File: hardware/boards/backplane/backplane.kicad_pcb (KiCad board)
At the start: 4 copper layers, 151.8 x 30.8 mm, 89 parts, among them J1 XT30U_2+2, J10 SWD, J11 12V 3-WIRE FAN, J12 DS18B20 EXT SUPPLY, J2 XT30U_2+2, J3 XT30U_2+2, J4 XT30U_2+2, J5 XT30U_2+2, J6 XT30U_2+2, J7 XY308-2.54-3P / EXTERNAL CAN, J8 DC IN, J9 12V 3-WIRE FAN, Q1 AO3407A, Q2 2N7002, Q3 AO3407A, Q4 2N7002, U1 STM32C092GCU6, U2 LM5164DDAR, U3 LM5164DDAR, U4 INA237AIDGSR, U5 TCAN3413DR

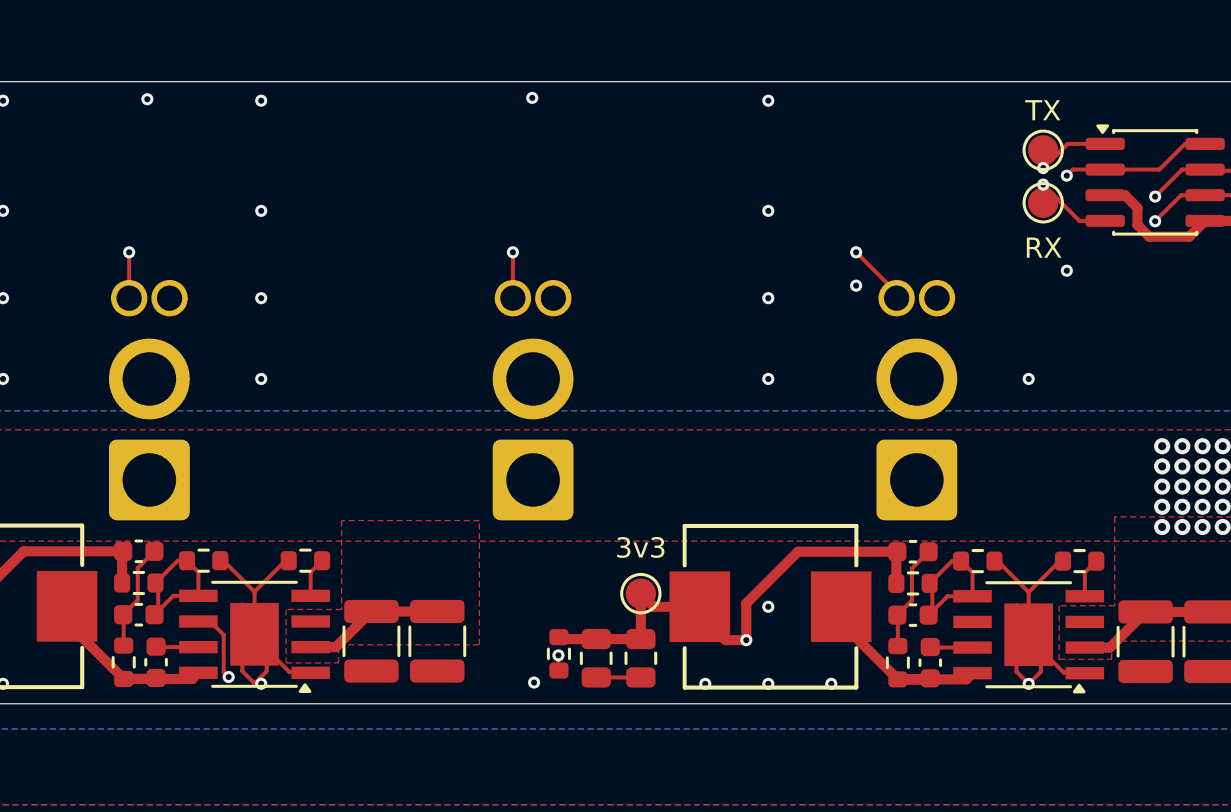
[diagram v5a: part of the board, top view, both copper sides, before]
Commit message: Checkpoint backplane before CAN test point routing adjustments
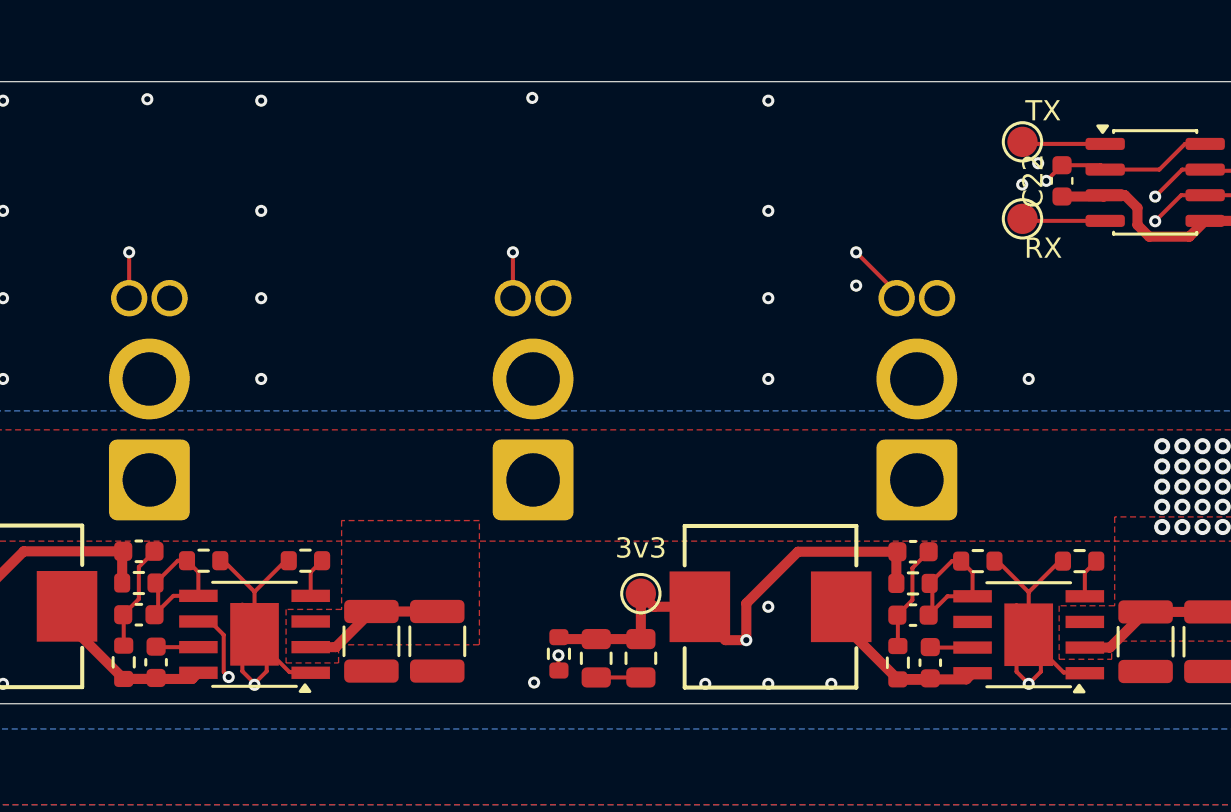
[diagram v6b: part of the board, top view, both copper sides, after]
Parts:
- added C22: 100nF, Capacitor_SMD:C_0603_1608Metric, F.Cu at (149.2, 51.6)
- moved TP7 1.30 mm to (147.2, 53.5)
- moved TP6 1.11 mm to (147.2, 49.7)
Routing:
- net +3V3: track 291.9 -> 294.0 mm
- net GND: track 56.7 -> 57.7 mm, vias 67 -> 66
- net CAN_RX: track 94.3 -> 93.5 mm

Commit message: Align CAN test points and clean up U5 routing and silkscreen
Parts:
- moved TP6 2.04 mm to (145.2, 49.8)
- moved TP7 2.04 mm to (145.2, 53.6)
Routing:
- net CAN_RX: track 93.5 -> 94.3 mm
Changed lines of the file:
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@@
 	(footprint "TestPoint:TestPoint_Pad_D1.5mm"
 		(layer "F.Cu")
-		(at 147.23576 49.682439)
+		(at 145.2 49.782989)
 		(descr "SMD pad as test Point, diameter 1.5mm")
 		(tags "test point SMD pad")
@@
 		(sheetname "/MCU and Local Control/")
 		(sheetfile "02_control.kicad_sch")
-		(units
-			(unit
-				(name "A")
-				(pins "1")
-			)
-		)
 		(attr exclude_from_bom dnp)
 		(duplicate_pad_numbers_are_jumpers no)
@@
 	(footprint "TestPoint:TestPoint_Pad_D1.5mm"
 		(layer "F.Cu")
-		(at 147.23576 53.492439)
+		(at 145.2 53.592989)
 		(descr "SMD pad as test Point, diameter 1.5mm")
 		(tags "test point SMD pad")
@@
 		(sheetname "/MCU and Local Control/")
 		(sheetfile "02_control.kicad_sch")
-		(units
-			(unit
-				(name "A")
-				(pins "1")
-			)
-		)
 		(attr exclude_from_bom dnp)
 		(duplicate_pad_numbers_are_jumpers no)
@@
 			(end 0.14058 -0.51)
 			(stroke
-				(width 0.12)
+				(width 0.15)
 				(type solid)
 			)
@@
 			(end 0.14058 0.51)
 			(stroke
-				(width 0.12)
+				(width 0.15)
 				(type solid)
 			)
@@
 	)
 	(gr_text "TX"
-		(at 148.262296 48.152097 0)
+		(at 145.2 47.8 0)
 		(layer "F.SilkS" knockout)
 		(effects
@@
 	)
 	(gr_text "RX"
-		(at 148.262296 54.955393 0)
+		(at 145.2 55.85 0)
 		(layer "F.SilkS" knockout)
 		(effects
@@
 	)
 	(segment
-		(start 147.33631 49.782989)
-		(end 147.23576 49.682439)
+		(start 62.215587 48.320577)
+		(end 59.958372 48.320577)
 		(width 0.2)
 		(layer "F.Cu")
@@
 	)
 	(segment
-		(start 62.215587 48.320577)
-		(end 59.958372 48.320577)
+		(start 144.767011 49.782989)
+		(end 151.328966 49.782989)
 		(width 0.2)
 		(layer "F.Cu")
@@
 	)
 	(segment
-		(start 151.328966 49.782989)
-		(end 147.33631 49.782989)
+		(start 143.8 50.75)
+		(end 144.767011 49.782989)
 		(width 0.2)
 		(layer "F.Cu")
@@
 	)
 	(via
-		(at 148.011789 50.738722)
+		(at 143.8 50.75)
 		(size 0.6)
 		(drill 0.3)
 		(layers "F.Cu" "B.Cu")
-		(free yes)
 		(net "CAN_TX")
 	)
 	(segment
-		(start 147.721812 50.448745)
-		(end 148.011789 50.738722)
+		(start 143.498745 50.448745)
+		(end 143.8 50.75)
 		(width 0.2)
 		(layer "In2.Cu")
@@
 	)
 	(segment
-		(start 66.702998 50.71)
-		(end 66.98305 50.448745)
+		(start 66.98305 50.448745)
+		(end 143.498745 50.448745)
 		(width 0.2)
 		(layer "In2.Cu")
@@
 	)
 	(segment
-		(start 66.98305 50.448745)
-		(end 147.721812 50.448745)
+		(start 66.702998 50.71)
+		(end 66.98305 50.448745)
 		(width 0.2)
 		(layer "In2.Cu")
@@
 	)
 	(segment
-		(start 66.702998 51.527071)
-		(end 64.80349 51.527071)
+		(start 143.8 53.592989)
+		(end 151.328966 53.592989)
 		(width 0.2)
 		(layer "F.Cu")
@@
 	)
 	(segment
-		(start 64.80349 51.527071)
-		(end 62.12557 48.849151)
+		(start 66.702998 51.527071)
+		(end 64.80349 51.527071)
 		(width 0.2)
 		(layer "F.Cu")
@@
 	)
 	(segment
-		(start 151.328966 53.592989)
-		(end 147.33631 53.592989)
+		(start 64.80349 51.527071)
+		(end 62.12557 48.849151)
 		(width 0.2)
 		(layer "F.Cu")
@@
 		(net "CAN_RX")
 	)
-	(segment
-		(start 147.33631 53.592989)
-		(end 147.23576 53.492439)
-		(width 0.2)
-		(layer "F.Cu")
-		(net "CAN_RX")
-	)
 	(via
-		(at 147.220393 51.796017)
+		(at 143.8 53.592989)
 		(size 0.6)
 		(drill 0.3)
 		(layers "F.Cu" "B.Cu")
-		(free yes)
 		(net "CAN_RX")
 	)
@@
 	)
 	(segment
-		(start 143.4064 50.848745)
-		(end 67.484209 50.848745)
-		(width 0.2)
-		(layer "In2.Cu")
-		(net "CAN_RX")
-	)
-	(segment
-		(start 143.696196 51.138541)
-		(end 143.4064 50.848745)
-		(width 0.2)
-		(layer "In2.Cu")
-		(net "CAN_RX")
-	)
-	(segment
-		(start 147.220393 51.796017)
-		(end 146.562917 51.138541)
+		(start 141.055756 50.848745)
+		(end 143.8 53.592989)
 		(width 0.2)
 		(layer "In2.Cu")
@@
 	)
 	(segment
-		(start 146.562917 51.138541)
-		(end 143.696196 51.138541)
+		(start 67.484209 50.848745)
+		(end 141.055756 50.848745)
 		(width 0.2)
 		(layer "In2.Cu")
